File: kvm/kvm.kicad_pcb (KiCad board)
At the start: 4 copper layers, 57 x 69.3 mm, 61 parts, among them J1 USB4110-GF-A, J2 USB4110-GF-A, J3 USB_A_Stacked, J4 USB_A_Stacked, Q1 Q_PMOS_GSD, SW1 SW_DPDT_x2, U1 SRV05-4, U2 LTC4412xS6, U3 FSUSB42MUX, U4 GL850G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

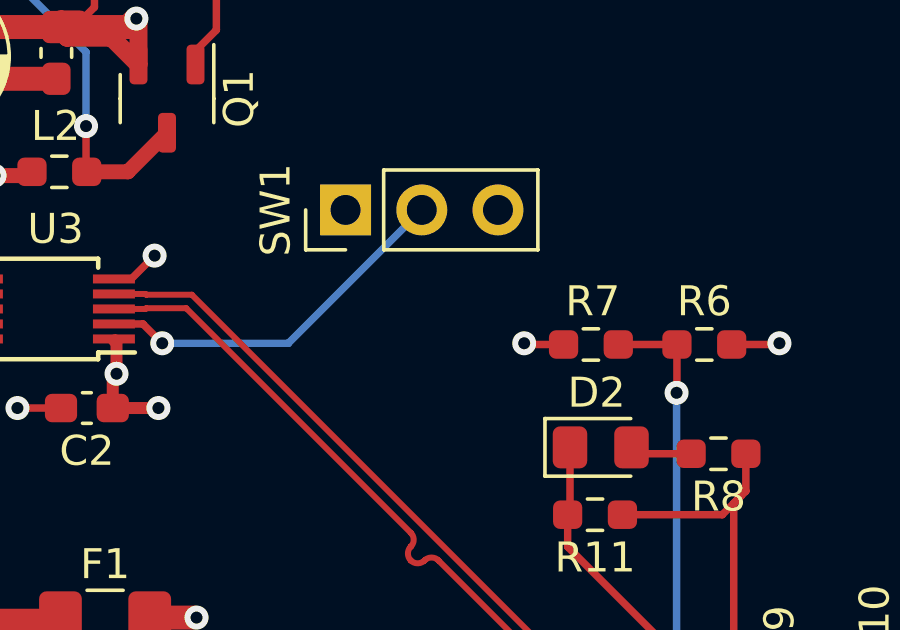
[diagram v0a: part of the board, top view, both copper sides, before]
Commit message: fixed missing pull down on FSUSBMUX
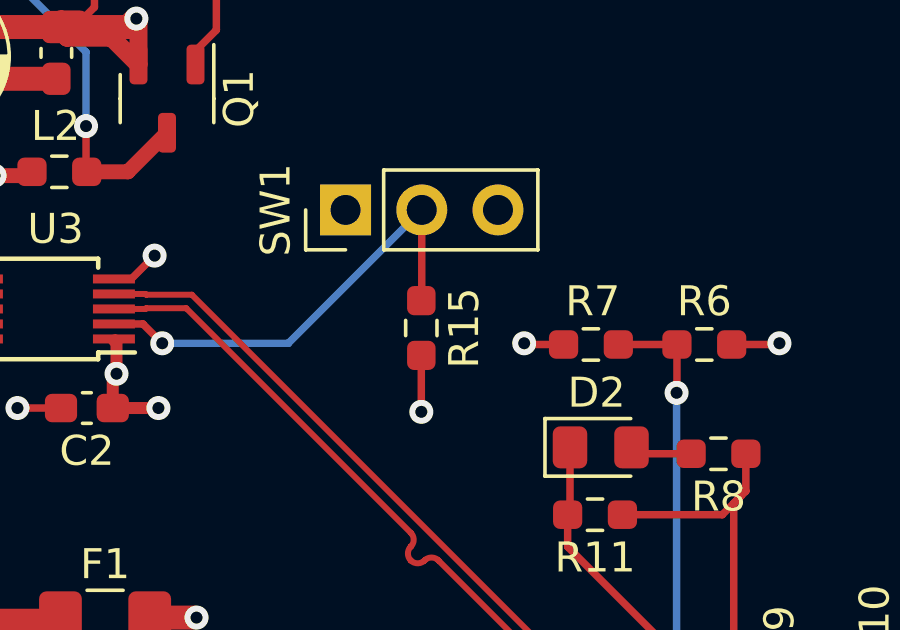
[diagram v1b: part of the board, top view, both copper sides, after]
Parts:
- added R15: 10K, Resistor_SMD:R_0603_1608Metric_Pad0.98x0.95mm_HandSolder, F.Cu at (97.5, 58.5)
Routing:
- net Net-(R15-Pad1): track 12.4 -> 15.4 mm
- net GND: track 73.2 -> 75.1 mm, vias 35 -> 36
